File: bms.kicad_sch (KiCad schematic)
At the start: 29 parts, among them Q1 SSM6K513NU-LF, Q2 SSM6K513NU-LF, Q3 2N7002W, U1 BQ28Z620DRZR

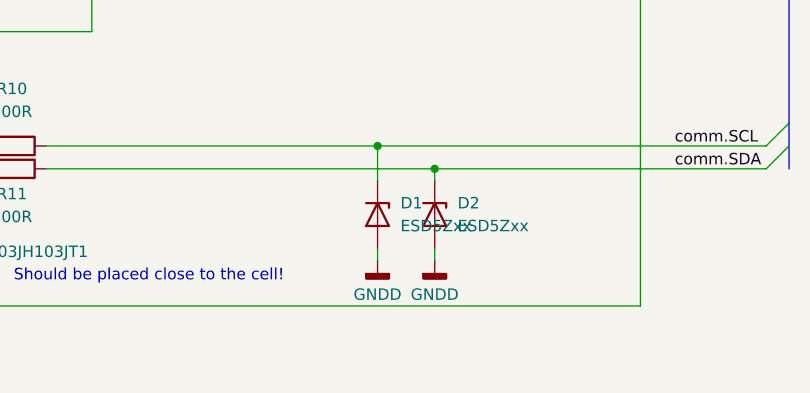
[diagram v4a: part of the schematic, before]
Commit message: Layout is finished with adding analog part, wiring the MCU ports and adding GNDD zones. Also add the nettie.
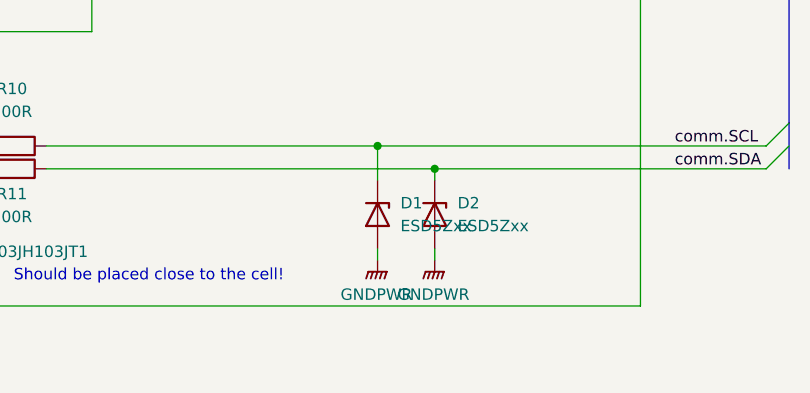
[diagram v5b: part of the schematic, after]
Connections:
- net GNDD is gone; now on net GNDPWR: D1.2 (A), D2.2 (A)
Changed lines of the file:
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@@
+	)
+	(symbol
+		(lib_id "power:GNDPWR")
+		(at 209.55 109.22 0)
+		(unit 1)
+		(body_style 1)
+		(exclude_from_sim no)
+		(in_bom yes)
+		(on_board yes)
+		(in_pos_files yes)
+		(dnp no)
+		(fields_autoplaced yes)
+		(property "Reference" "#PWR071"
+			(at 209.55 114.3 0)
+			(hide yes)
+			(show_name no)
+			(do_not_autoplace no)
+			(effects
+				(font
+					(size 1.27 1.27)
+				)
+			)
+		)
+		(property "Value" "GNDPWR"
+			(at 209.423 113.03 0)
+			(show_name no)
+			(do_not_autoplace no)
+			(effects
+				(font
+					(size 1.27 1.27)
+				)
+			)
+		)
+		(property "Footprint" ""
+			(at 209.55 110.49 0)
+			(hide yes)
+			(show_name no)
+			(do_not_autoplace no)
+			(effects
+				(font
+					(size 1.27 1.27)
+				)
+			)
+		)
+		(property "Datasheet" ""
+			(at 209.55 110.49 0)
+			(hide yes)
+			(show_name no)
+			(do_not_autoplace no)
+			(effects
+				(font
+					(size 1.27 1.27)
+				)
+			)
+		)
+		(property "Description" "Power symbol creates a global label with name \"GNDPWR\" , global ground"
+			(at 209.55 109.22 0)
+			(hide yes)
+			(show_name no)
+			(do_not_autoplace no)
+			(effects
+				(font
+					(size 1.27 1.27)
+				)
+			)
+		)
+		(pin "1"
+		)
+		(instances
+			(project "MoistureESP"
+				(path "/f2b9f638-139e-46ec-aa60-77c4af989196/b13ba67b-4069-4f36-b5d0-6a46a6b78ce9"
+					(reference "#PWR071")
+					(unit 1)
+				)
+			)
+		)
 	)
 	(symbol
@@
 	)
 	(symbol
-		(lib_id "power:GNDD")
-		(at 209.55 109.22 0)
-		(unit 1)
-		(body_style 1)
-		(exclude_from_sim no)
-		(in_bom yes)
-		(on_board yes)
-		(in_pos_files yes)
-		(dnp no)
-		(fields_autoplaced yes)
-		(property "Reference" "#PWR024"
-			(at 209.55 115.57 0)
-			(hide yes)
-			(show_name no)
-			(do_not_autoplace no)
-			(effects
-				(font
-					(size 1.27 1.27)
-				)
-			)
-		)
-		(property "Value" "GNDD"
-			(at 209.55 113.03 0)
+		(lib_id "power:GNDPWR")
+		(at 215.9 109.22 0)
+		(unit 1)
+		(body_style 1)
+		(exclude_from_sim no)
+		(in_bom yes)
+		(on_board yes)
+		(in_pos_files yes)
+		(dnp no)
+		(fields_autoplaced yes)
+		(property "Reference" "#PWR072"
+			(at 215.9 114.3 0)
+			(hide yes)
+			(show_name no)
+			(do_not_autoplace no)
+			(effects
+				(font
+					(size 1.27 1.27)
+				)
+			)
+		)
+		(property "Value" "GNDPWR"
+			(at 215.773 113.03 0)
 			(show_name no)
 			(do_not_autoplace no)
@@
 		)
 		(property "Footprint" ""
-			(at 209.55 109.22 0)
-			(hide yes)
-			(show_name no)
-			(do_not_autoplace no)
-			(effects
-				(font
-					(size 1.27 1.27)
-				)
-			)
-		)
-		(property "Datasheet" ""
-			(at 209.55 109.22 0)
-			(hide yes)
-			(show_name no)
-			(do_not_autoplace no)
-			(effects
-				(font
-					(size 1.27 1.27)
-				)
-			)
-		)
-		(property "Description" "Power symbol creates a global label with name \"GNDD\" , digital ground"
-			(at 209.55 109.22 0)
-			(hide yes)
-			(show_name no)
-			(do_not_autoplace no)
-			(effects
-				(font
-					(size 1.27 1.27)
-				)
-			)
-		)
-		(pin "1"
-		)
-		(instances
-			(project "MoistureESP"
-				(path "/f2b9f638-139e-46ec-aa60-77c4af989196/b13ba67b-4069-4f36-b5d0-6a46a6b78ce9"
-					(reference "#PWR024")
+			(at 215.9 110.49 0)
+			(hide yes)
+			(show_name no)
+			(do_not_autoplace no)
+			(effects
+				(font
+					(size 1.27 1.27)
+				)
+			)
+		)
+		(property "Datasheet" ""
+			(at 215.9 110.49 0)
+			(hide yes)
+			(show_name no)
+			(do_not_autoplace no)
+			(effects
+				(font
+					(size 1.27 1.27)
+				)
+			)
+		)
+		(property "Description" "Power symbol creates a global label with name \"GNDPWR\" , global ground"
+			(at 215.9 109.22 0)
+			(hide yes)
+			(show_name no)
+			(do_not_autoplace no)
+			(effects
+				(font
+					(size 1.27 1.27)
+				)
+			)
+		)
+		(pin "1"
+		)
+		(instances
+			(project "MoistureESP"
+				(path "/f2b9f638-139e-46ec-aa60-77c4af989196/b13ba67b-4069-4f36-b5d0-6a46a6b78ce9"
+					(reference "#PWR072")
 					(unit 1)
 				)
@@
 					(unit 1)
 				)
-			)
-		)
-	)
-	(symbol
-		(lib_id "power:GNDD")
-		(at 215.9 109.22 0)
-		(unit 1)
-		(body_style 1)
-		(exclude_from_sim no)
-		(in_bom yes)
-		(on_board yes)
-		(in_pos_files yes)
-		(dnp no)
-		(fields_autoplaced yes)
-		(property "Reference" "#PWR025"
-			(at 215.9 115.57 0)
-			(hide yes)
-			(show_name no)
-			(do_not_autoplace no)
-			(effects
-				(font
-					(size 1.27 1.27)
-				)
-			)
-		)
-		(property "Value" "GNDD"
-			(at 215.9 113.03 0)
-			(show_name no)
-			(do_not_autoplace no)
-			(effects
-				(font
-					(size 1.27 1.27)
-				)
-			)
-		)
-		(property "Footprint" ""
-			(at 215.9 109.22 0)
-			(hide yes)
-			(show_name no)
-			(do_not_autoplace no)
-			(effects
-				(font
-					(size 1.27 1.27)
-				)
-			)
-		)
-		(property "Datasheet" ""
-			(at 215.9 109.22 0)
-			(hide yes)
-			(show_name no)
-			(do_not_autoplace no)
-			(effects
-				(font
-					(size 1.27 1.27)
-				)
-			)
-		)
-		(property "Description" "Power symbol creates a global label with name \"GNDD\" , digital ground"
-			(at 215.9 109.22 0)
-			(hide yes)
-			(show_name no)
-			(do_not_autoplace no)
-			(effects
-				(font
-					(size 1.27 1.27)
-				)
-			)
-		)
-		(pin "1"
-		)
-		(instances
-			(project "MoistureESP"
-				(path "/f2b9f638-139e-46ec-aa60-77c4af989196/b13ba67b-4069-4f36-b5d0-6a46a6b78ce9"
-					(reference "#PWR025")
-					(unit 1)
-				)

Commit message: Export BOM, change page headers.
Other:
- company: (none) -> B.Major
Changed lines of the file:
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@@
 	(generator_version "10.0")
 	(paper "A4")
+	(title_block
+		(date "2026-03-27")
+		(rev "1")
+		(company "B.Major")
+	)
 	(text "Should be placed close to the cell!"
 		(exclude_from_sim no)
